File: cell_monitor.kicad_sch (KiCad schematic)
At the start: 48 parts, among them Q10 BUK7M67-60EX, Q11 BUK7M67-60EX, Q8 AO3401A, SW2 SW_Push, U3 BQ76920PW, U4 BQ76200PW

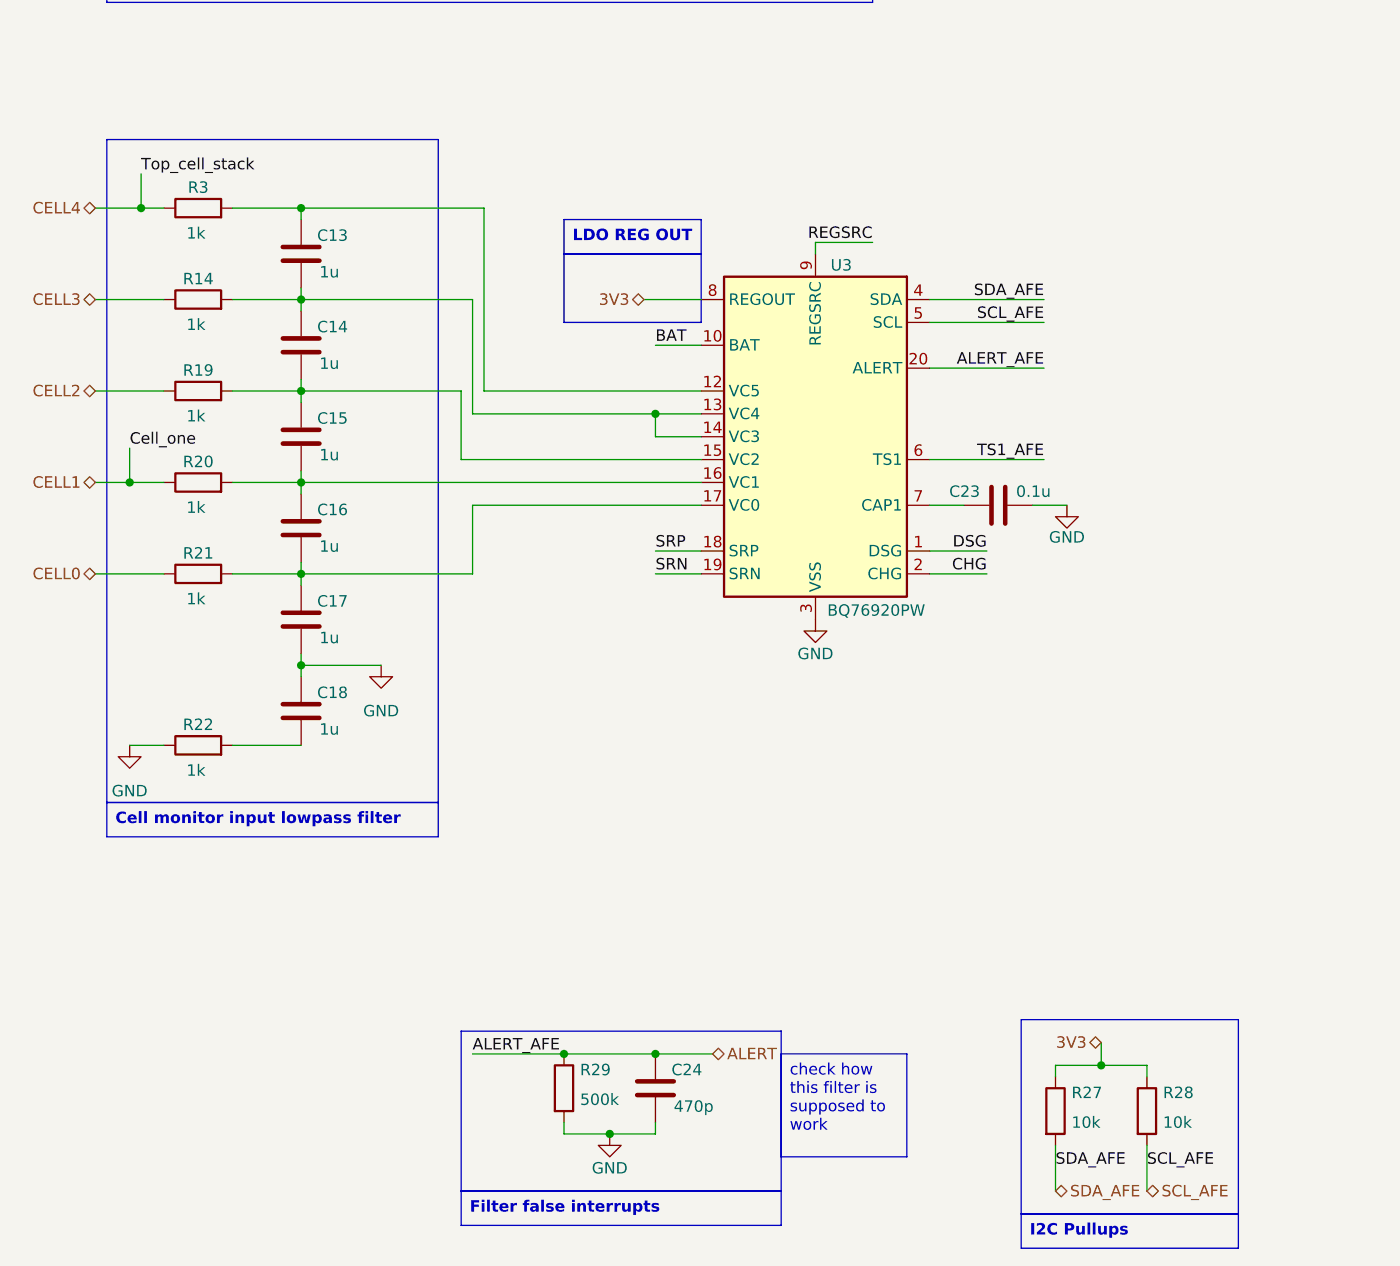
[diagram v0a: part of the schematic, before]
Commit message: beginning fuel gage layout
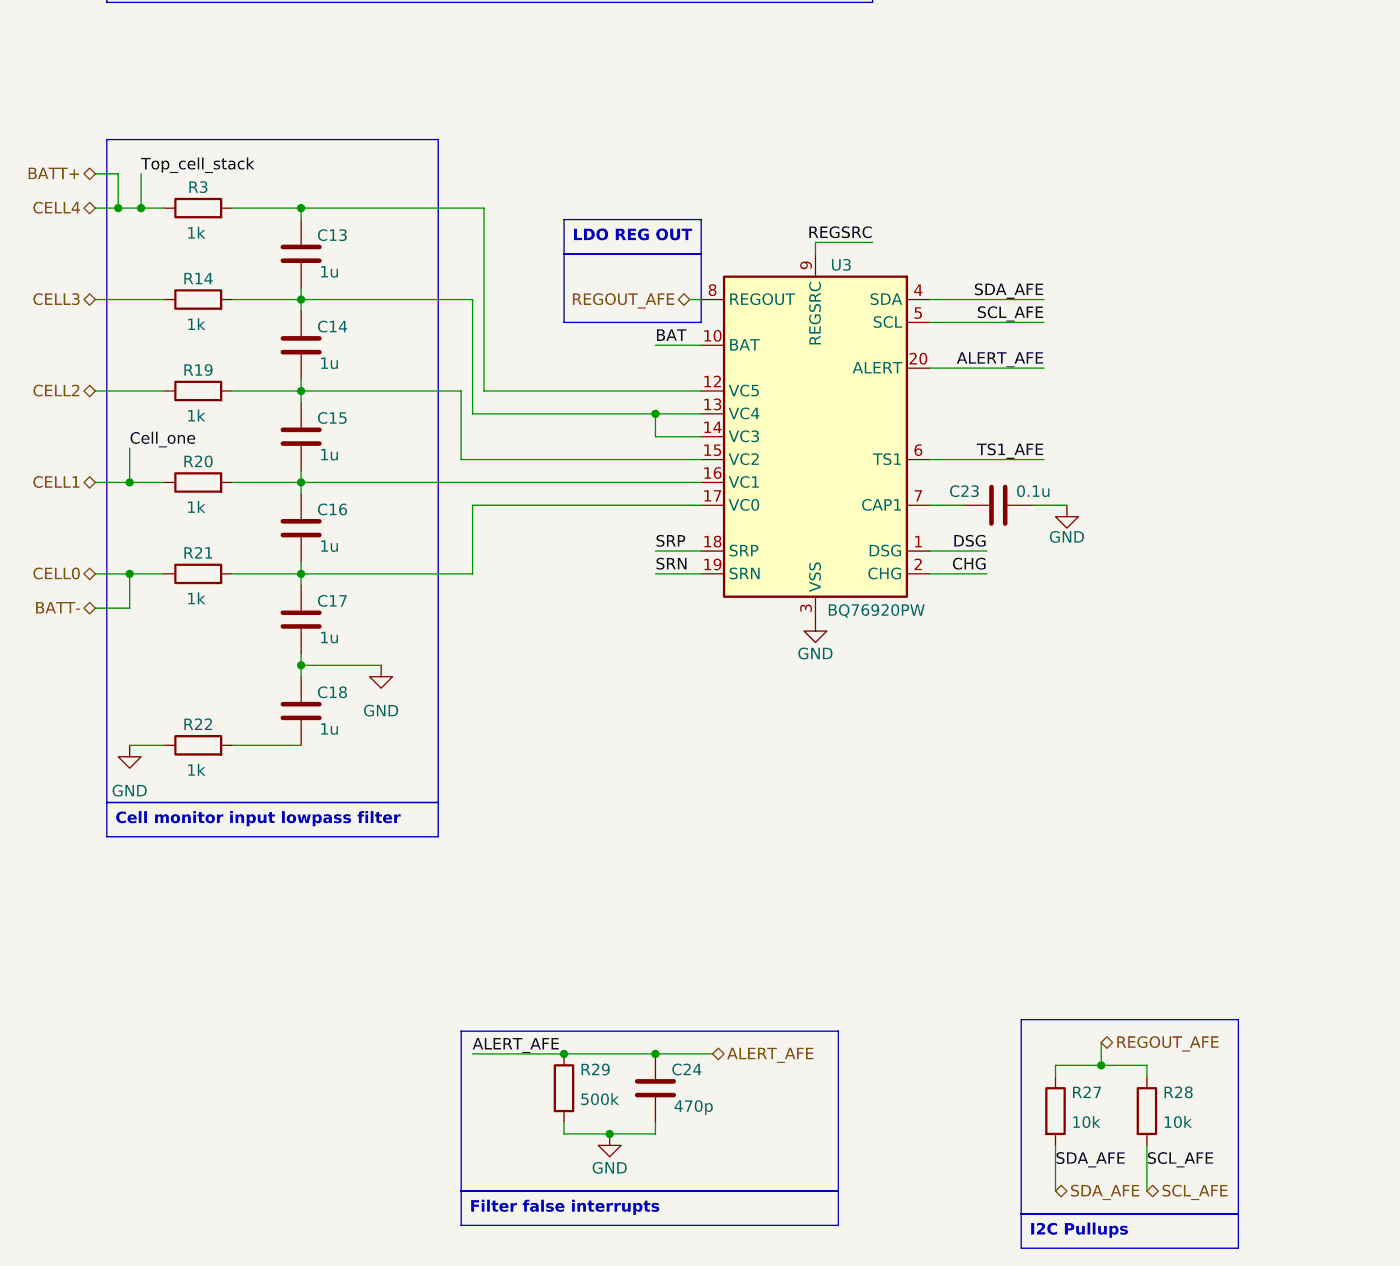
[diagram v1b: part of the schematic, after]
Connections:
- net 3V3 renamed REGOUT_AFE
- net ALERT renamed ALERT_AFE
- net CELL0 renamed BATT-
- net CELL4 renamed BATT+
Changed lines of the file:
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@@
 	(rectangle
 		(start 62.23 166.37)
-		(end 97.79 184.15)
+		(end 104.14 184.15)
 		(stroke
 			(width 0)
@@
 		)
 	)
-	(text_box "check how this filter is supposed to work"
-		(exclude_from_sim no)
-		(at 97.79 168.91 0)
-		(size 13.97 11.43)
-		(margins 0.9525 0.9525 0.9525 0.9525)
-		(stroke
-			(width 0)
-			(type solid)
-		)
-		(fill
-			(type color)
-			(color 255 250 158 1)
-		)
-		(effects
-			(font
-				(size 1.27 1.27)
-				(thickness 0.1588)
-			)
-			(justify left top)
-		)
-	)
 	(text_box "Startup / Temperature sensing"
 		(exclude_from_sim no)
@@
 		(exclude_from_sim no)
 		(at 62.23 184.15 0)
-		(size 35.56 3.81)
+		(size 41.91 3.81)
 		(margins 0.9525 0.9525 0.9525 0.9525)
 		(stroke
@@
 	)
 	(junction
+		(at 25.4 115.57)
+		(diameter 0)
+		(color 0 0 0 0)
+	)
+	(junction
 		(at 73.66 168.91)
 		(diameter 0)
@@
 	)
 	(junction
+		(at 24.13 74.93)
+		(diameter 0)
+		(color 0 0 0 0)
+	)
+	(junction
 		(at 83.82 97.79)
 		(diameter 0)
@@
 	(wire
 		(pts
+			(xy 21.59 119.38) (xy 25.4 119.38)
+		)
+		(stroke
+			(width 0)
+			(type default)
+		)
+	)
+	(wire
+		(pts
 			(xy 125.73 107.95) (xy 129.54 107.95)
 		)
@@
 	(wire
 		(pts
+			(xy 25.4 115.57) (xy 29.21 115.57)
+		)
+		(stroke
+			(width 0)
+			(type default)
+		)
+	)
+	(wire
+		(pts
 			(xy 205.74 49.53) (xy 205.74 52.07)
 		)
@@
 	(wire
 		(pts
+			(xy 24.13 74.93) (xy 26.67 74.93)
+		)
+		(stroke
+			(width 0)
+			(type default)
+		)
+	)
+	(wire
+		(pts
 			(xy 232.41 83.82) (xy 236.22 83.82)
 		)
@@
 	(wire
 		(pts
+			(xy 24.13 71.12) (xy 24.13 74.93)
+		)
+		(stroke
+			(width 0)
+			(type default)
+		)
+	)
+	(wire
+		(pts
 			(xy 210.82 33.02) (xy 213.36 33.02)
 		)
@@
 	(wire
 		(pts
+			(xy 21.59 71.12) (xy 24.13 71.12)
+		)
+		(stroke
+			(width 0)
+			(type default)
+		)
+	)
+	(wire
+		(pts
 			(xy 200.66 41.91) (xy 212.09 41.91)
 		)
@@
 	(wire
 		(pts
-			(xy 21.59 74.93) (xy 26.67 74.93)
+			(xy 25.4 119.38) (xy 25.4 115.57)
+		)
+		(stroke
+			(width 0)
+			(type default)
+		)
+	)
+	(wire
+		(pts
+			(xy 21.59 74.93) (xy 24.13 74.93)
 		)
 		(stroke
@@
 	(wire
 		(pts
-			(xy 21.59 115.57) (xy 29.21 115.57)
+			(xy 21.59 115.57) (xy 25.4 115.57)
 		)
 		(stroke
@@
 	(wire
 		(pts
-			(xy 82.55 85.09) (xy 88.9 85.09)
+			(xy 87.63 85.09) (xy 88.9 85.09)
 		)
 		(stroke
@@
 			)
 			(justify right bottom)
+		)
+	)
+	(hierarchical_label "BATT-"
+		(shape bidirectional)
+		(at 21.59 119.38 180)
+		(effects
+			(font
+				(size 1.27 1.27)
+			)
+			(justify right)
 		)
 	)
@@
 		)
 	)
+	(hierarchical_label "BATT+"
+		(shape bidirectional)
+		(at 21.59 71.12 180)
+		(effects
+			(font
+				(size 1.27 1.27)
+			)
+			(justify right)
+		)
+	)
 	(hierarchical_label "PACK-"
 		(shape bidirectional)
@@
 		)
 	)
-	(hierarchical_label "3V3"
+	(hierarchical_label "REGOUT_AFE"
 		(shape bidirectional)
-		(at 133.35 167.64 180)
-		(effects
-			(font
-				(size 1.27 1.27)
-			)
-			(justify right)
-		)
-	)
-	(hierarchical_label "3V3"
-		(shape bidirectional)
-		(at 82.55 85.09 180)
+		(at 87.63 85.09 180)
 		(effects
 			(font
@@
 		)
 	)
-	(hierarchical_label "ALERT"
+	(hierarchical_label "ALERT_AFE"
 		(shape bidirectional)
 		(at 90.17 168.91 0)
@@
 		)
 	)
+	(hierarchical_label "REGOUT_AFE"
+		(shape bidirectional)
+		(at 133.35 167.64 0)
+		(effects
+			(font
+				(size 1.27 1.27)
+			)
+			(justify left)
+		)
+	)

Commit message: .
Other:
- note removed: "HS_SW = HIGHSIDE SWITCHING - referring to BQ76200PW high side switching driver"
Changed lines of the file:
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@@
-		)
-	)
-	(text "HS_SW = HIGHSIDE SWITCHING - \nreferring to BQ76200PW high side switching driver"
-		(exclude_from_sim no)
-		(at 250.19 171.45 0)
-		(effects
-			(font
-				(size 1.27 1.27)
-			)
 		)
 	)
@@
 	(text_box "maxiumum expected current - max power draw estimate 70W - at nominal voltage approx 3x3.6=10.8V - max currents expected approx 6.5A, will rate anything in main conduction path to 10A"
 		(exclude_from_sim no)
-		(at 184.15 166.37 0)
+		(at 16.51 162.56 0)
 		(size 41.91 15.24)
 		(margins 0.9525 0.9525 0.9525 0.9525)

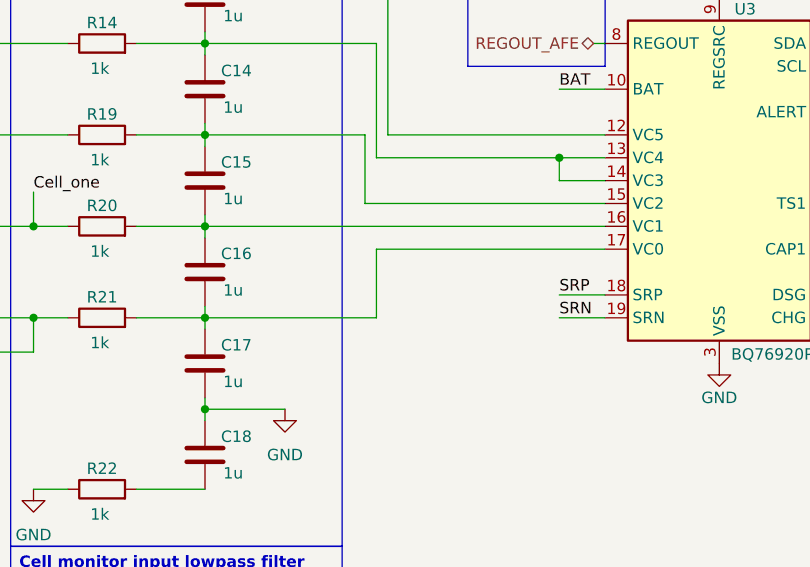
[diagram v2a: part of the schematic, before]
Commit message: starting usb pd charging
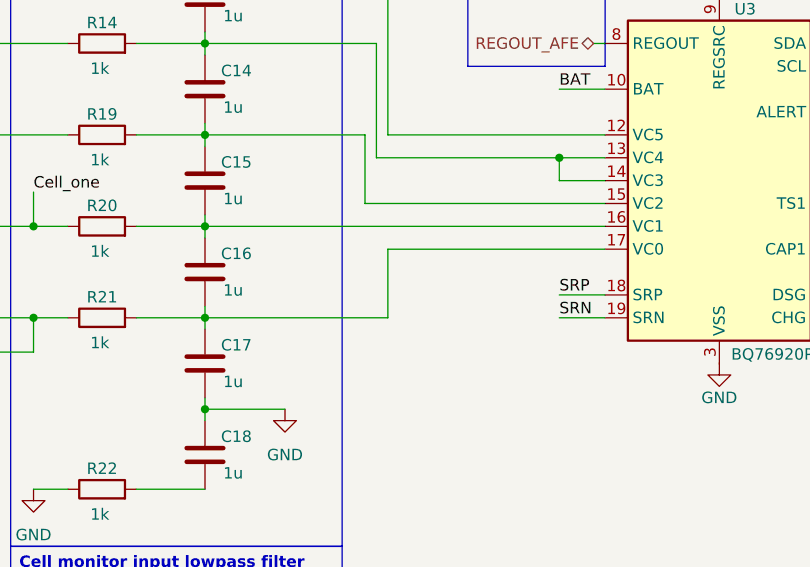
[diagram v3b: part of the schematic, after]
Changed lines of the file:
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@@
 	(wire
 		(pts
-			(xy 63.5 107.95) (xy 88.9 107.95)
+			(xy 64.77 107.95) (xy 88.9 107.95)
 		)
 		(stroke
@@
 	(wire
 		(pts
-			(xy 63.5 115.57) (xy 63.5 107.95)
+			(xy 64.77 115.57) (xy 64.77 107.95)
 		)
 		(stroke
@@
 	(wire
 		(pts
-			(xy 44.45 115.57) (xy 63.5 115.57)
-		)
-		(stroke
+			(xy 44.45 115.57) (xy 64.77 115.57)
+		)
+		(stroke

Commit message: usb pd charging
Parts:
- added C6: 1u, symbol Device:C
- added R9: 1k, symbol Device:R
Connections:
- net CELL3: now also R9.1; no longer R14.1
- net at C13.2, C14.1, R14.2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: no longer U3.14 (VC3)
- net at C15.1, R19.2, U3.15 (VC2): now also C6.2; no longer C14.2
- new net: C14.2, C6.1, R9.2, U3.14 (VC3)
- new net CELL4: R14.1
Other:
- moved on the sheet: C13, C14, C23, R14, R3, U3

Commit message: progress
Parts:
- renumbered C13 to C37, C14 to C38, C6 to C39, C15 to C40, C16 to C41, C17 to C42, C18 to C43, C24 to C44, C23 to C50, C19 to C51, C20 to C52, C21 to C53, CVDDCP_HS_SW to CVDDCP_HS_SW1, Cfilter to Cfilter1, Cfilter_HS_SW_BAT to Cfilter_HS_SW_BAT1, Csrc to Csrc1, D4 to D1, Q8 to Q7, Q11 to Q8, Q10 to Q9, R3 to R25, R14 to R26, R9 to R27, R19 to R28, R20 to R29, R21 to R30, R22 to R31, R29 to R32, R27 to R33, R28 to R34, R32 to R35, R23 to R36, R24 to R37, R1 to R38, R2 to R39, R25 to R40, RGS_HS_SW_CH to RGS_HS_SW_CH1, RGS_HS_SW_DCH to RGS_HS_SW_DCH1, RGS_HS_SW_PCHG to RGS_HS_SW_PCHG1, R_filter to R_filter1, Rd_AFE_REGSRC to Rd_AFE_REGSRC1, Rf_AFE_BATT to Rf_AFE_BATT1, Rfilter_HS_SW_BAT to Rfilter_HS_SW_BAT1, Rpchg_HS_SW to Rpchg_HS_SW1, Rsrc_AFE_REGSRC to Rsrc_AFE_REGSRC1, SW2 to SW1, TH2 to TH1, U4 to U5
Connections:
- net BATT+ renamed CELL5
- net BATT- renamed CELL0

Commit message: updates
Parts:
- removed C42, C43: 1u, symbol Device:C
- removed R30, R31: 1k, symbol Device:R
- added C7: 1u, symbol Device:C
- added R16: 1k, symbol Device:R
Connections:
- net GND: now also C41.2, U3.17 (VC0), C7.1, R16.1
- new net: C7.2, R16.2
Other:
- note added: "should this be used?"

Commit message: development stage 1 - testing board for AFE / Fuel gage / high side protection controller - unfinished
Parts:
- removed Csrc1: 1, symbol Device:C
- removed Rsrc_AFE_REGSRC1: R, symbol Device:R
- added TP2: TestPoint, symbol Connector:TestPoint
- Cf1: value 10u -> 2.2u
- D1: value D -> 100V
- R38: value R -> 300k
- R39: value R -> 16k
- Rd_AFE_REGSRC1: value R -> 10k
- Rsense: renamed from R37; value R sense -> 15m
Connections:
- net REGSRC is gone; now on net BAT: U3.9 (REGSRC)
- net GND: now also C7.2; no longer C41.2, C7.1, U3.17 (VC0)
- net HS_SW_PACKDIV: now also TP2.1
- net at R16.2: now also C41.2, C7.1, U3.17 (VC0); no longer C7.2
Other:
- note added: "1k inline resistors will limit balancing currents"
- note added: "20mA limit- NOT efficient - stated in page 21 of USER GUIDE"
- note added: "75ppm"
- note removed: "should this be used?"
- moved on the sheet: R16, Rf_AFE_BATT1

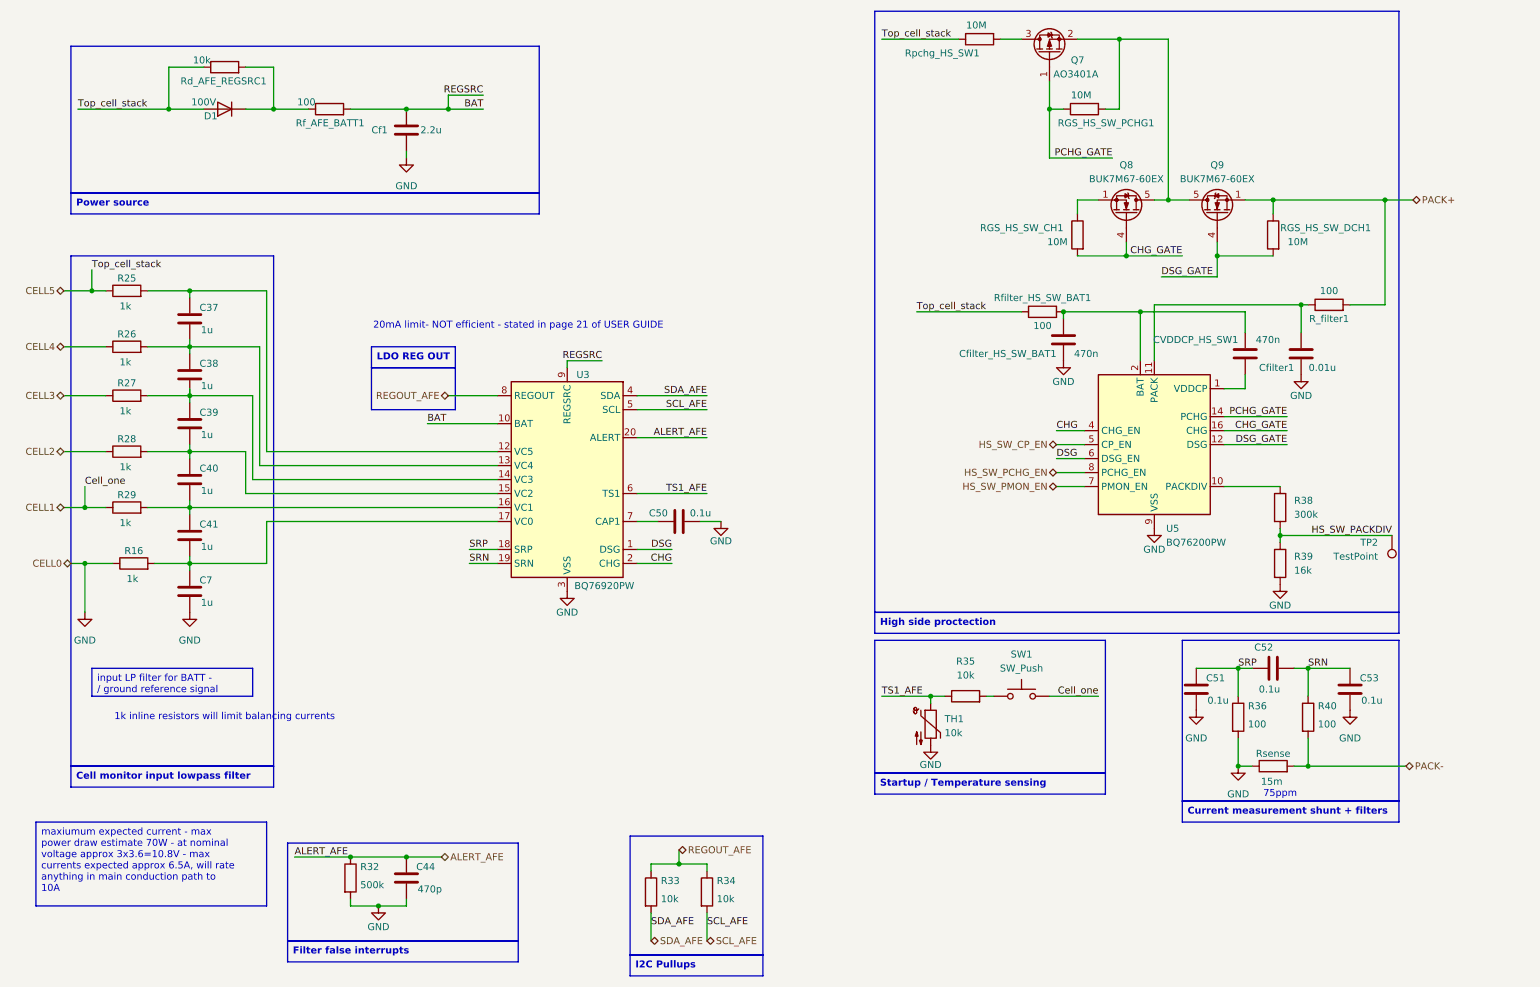
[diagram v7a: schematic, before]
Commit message: refinements - moving battery pack off the PCB
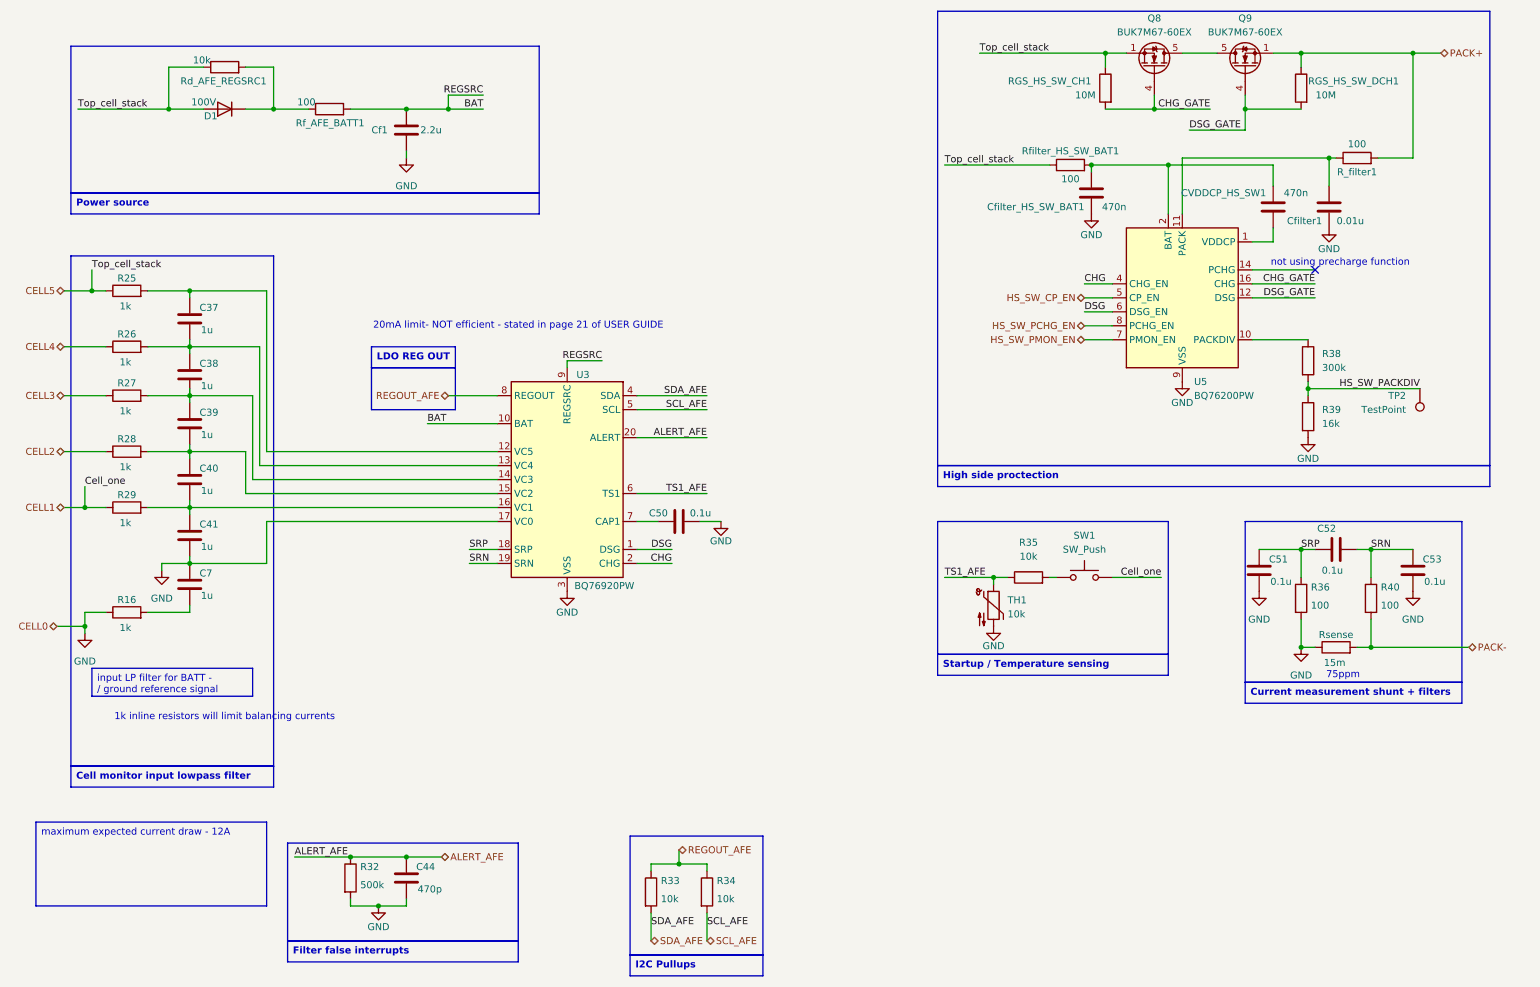
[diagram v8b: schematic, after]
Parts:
- removed Q7: AO3401A, Package_TO_SOT_SMD:SOT-23, symbol Transistor_FET:AO3401A
- removed RGS_HS_SW_PCHG1, Rpchg_HS_SW1: 10M, symbol Device:R
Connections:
- net CELL5: now also Q8.1 (S), Q8.2 (S), Q8.3 (S), RGS_HS_SW_CH1.1
- net GND: now also C41.2, C7.1, U3.17 (VC0); no longer C7.2
- net PCHG_GATE: no longer names the net of U5.14 (PCHG)
- new net: C7.2, R16.2
- no-connect marks 0 -> 1
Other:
- note added: "not using precharge function"
- moved on the sheet: C51, C52, C53, C7, CVDDCP_HS_SW1, Cfilter1, Cfilter_HS_SW_BAT1, Q8, Q9, R16, R35, R36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
